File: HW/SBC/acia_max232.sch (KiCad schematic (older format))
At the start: 12 parts, among them J1 Serial Port, U4 MAX232, U5 6551

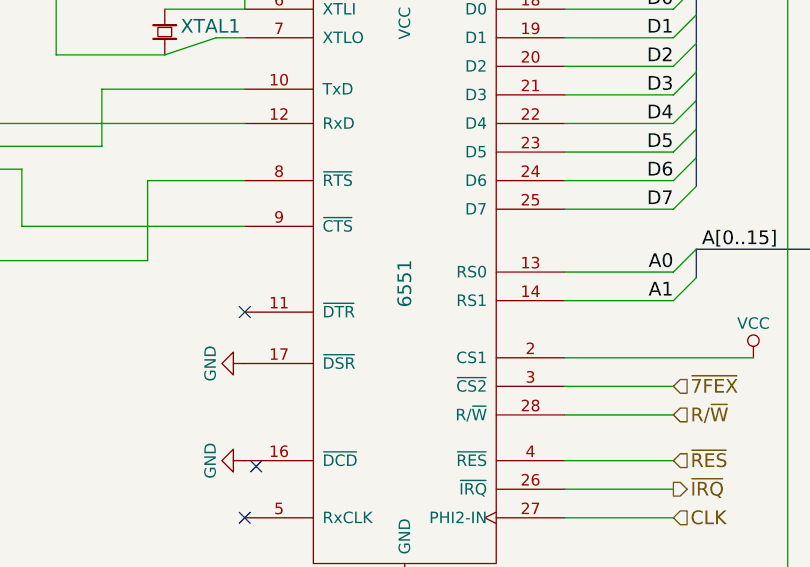
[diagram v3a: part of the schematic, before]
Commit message: Still no VCC net in PCBnew.
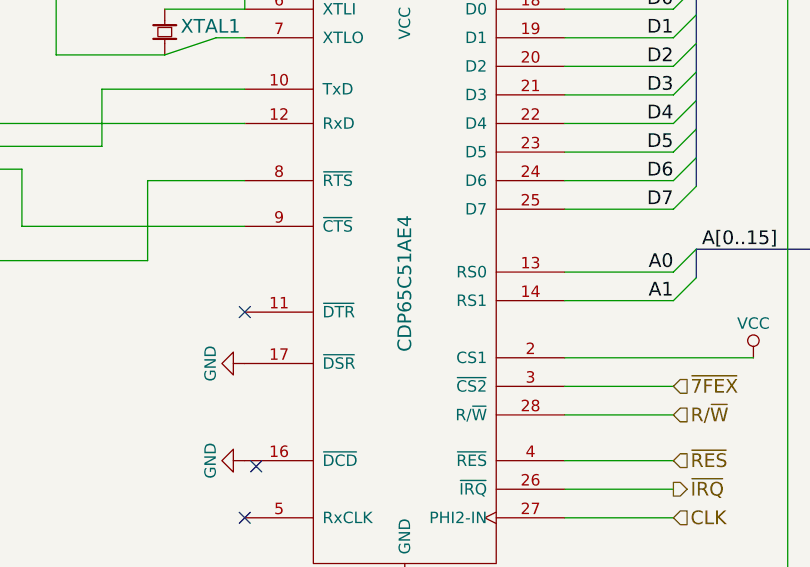
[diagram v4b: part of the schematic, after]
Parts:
- U4: footprint Housings_DIP:DIP-16_W7.62mm -> Housings_DIP:DIP-16_W7.62mm_Socket
- U5: value 6551 -> CDP65C51AE4; footprint Housings_DIP:DIP-28_W15.24mm -> Housings_DIP:DIP-28_W15.24mm_Socket
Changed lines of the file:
@@
 EESchema Schematic File Version 2
-LIBS:pluto-rescue
 LIBS:power
 LIBS:device
@@
 LIBS:pluto
 LIBS:pluto-cache
-LIBS:IDE_interface-cache
 EELAYER 25 0
 EELAYER END
@@
 P 7975 3150
 F 0 "U5" H 7750 4475 60  0000 C CNN
-F 1 "6551" V 7975 3150 60  0000 C CNN
-F 2 "Housings_DIP:DIP-28_W15.24mm" H 8025 2475 60  0001 C CNN
+F 1 "CDP65C51AE4" V 7975 3150 60  0000 C CNN
+F 2 "Housings_DIP:DIP-28_W15.24mm_Socket" H 8025 2475 60  0001 C CNN
 F 3 "" H 8025 2475 60  0001 C CNN
 	1    7975 3150
@@
 F 0 "U4" H 4950 2075 50  0000 R CNN
 F 1 "MAX232" H 4400 4200 50  0000 R CNN
-F 2 "Housings_DIP:DIP-16_W7.62mm" H 4550 2100 50  0001 L CNN
+F 2 "Housings_DIP:DIP-16_W7.62mm_Socket" H 4550 2100 50  0001 L CNN
 F 3 "" H 4500 3250 50  0001 C CNN
 	1    4500 3150

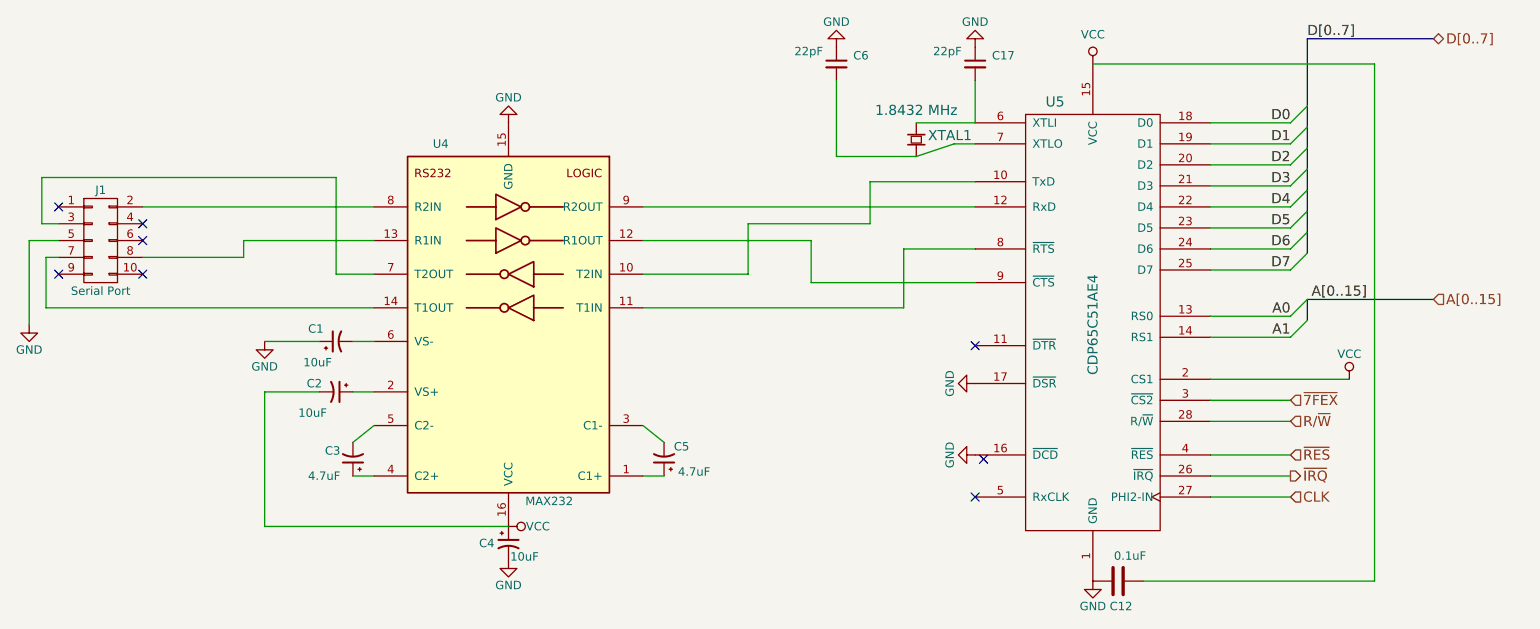
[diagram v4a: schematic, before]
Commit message: Schema is now Alpha.
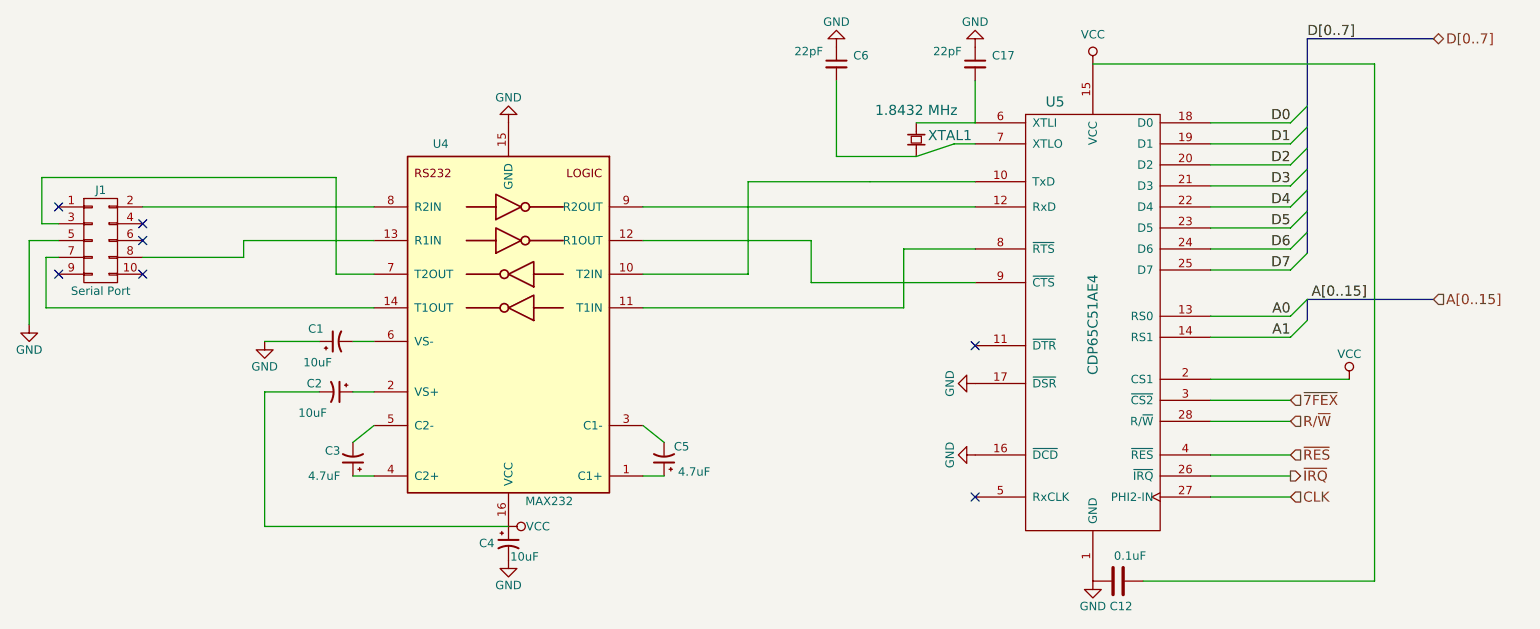
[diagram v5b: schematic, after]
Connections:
- no-connect marks 8 -> 7
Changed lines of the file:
@@
 $EndComp
 $Comp
-L VCC #PWR07
+L VCC #PWR18
 U 1 1 58D6F59A
 P 9500 3475
-F 0 "#PWR07" H 9500 3325 50  0001 C CNN
+F 0 "#PWR18" H 9500 3325 50  0001 C CNN
 F 1 "VCC" H 9500 3625 50  0000 C CNN
 F 2 "" H 9500 3475 50  0001 C CNN
@@
 $EndComp
 $Comp
-L GND #PWR08
+L GND #PWR12
 U 1 1 58D7044A
 P 6450 1500
-F 0 "#PWR08" H 6450 1250 50  0001 C CNN
+F 0 "#PWR12" H 6450 1250 50  0001 C CNN
 F 1 "GND" H 6450 1350 50  0000 C CNN
 F 2 "" H 6450 1500 50  0001 C CNN
@@
 $EndComp
 $Comp
-L GND #PWR09
+L GND #PWR8
 U 1 1 58D716F3
 P 3050 3250
-F 0 "#PWR09" H 3050 3000 50  0001 C CNN
+F 0 "#PWR8" H 3050 3000 50  0001 C CNN
 F 1 "GND" H 3050 3100 50  0000 C CNN
 F 2 "" H 3050 3250 50  0001 C CNN
@@
 $EndComp
 $Comp
-L GND #PWR010
+L GND #PWR7
 U 1 1 58D71F12
 P 1650 3150
-F 0 "#PWR010" H 1650 2900 50  0001 C CNN
+F 0 "#PWR7" H 1650 2900 50  0001 C CNN
 F 1 "GND" H 1650 3000 50  0000 C CNN
 F 2 "" H 1650 3150 50  0001 C CNN
@@
 $EndComp
 $Comp
-L GND #PWR011
+L GND #PWR11
 U 1 1 58D72DB3
 P 4500 4550
-F 0 "#PWR011" H 4500 4300 50  0001 C CNN
+F 0 "#PWR11" H 4500 4300 50  0001 C CNN
 F 1 "GND" H 4500 4400 50  0000 C CNN
 F 2 "" H 4500 4550 50  0001 C CNN
@@
 $EndComp
 $Comp
-L GND #PWR012
+L GND #PWR9
 U 1 1 58D73252
 P 4500 1950
-F 0 "#PWR012" H 4500 1700 50  0001 C CNN
+F 0 "#PWR9" H 4500 1700 50  0001 C CNN
 F 1 "GND" H 4500 1800 50  0000 C CNN
 F 2 "" H 4500 1950 50  0001 C CNN
@@
 NoConn ~ 1825 2450
 $Comp
-L GND #PWR013
+L GND #PWR15
 U 1 1 58D744C7
 P 7275 3925
-F 0 "#PWR013" H 7275 3675 50  0001 C CNN
+F 0 "#PWR15" H 7275 3675 50  0001 C CNN
 F 1 "GND" H 7275 3775 50  0000 C CNN
 F 2 "" H 7275 3925 50  0001 C CNN
@@
 $EndComp
 $Comp
-L GND #PWR014
+L GND #PWR14
 U 1 1 58D74507
 P 7275 3500
-F 0 "#PWR014" H 7275 3250 50  0001 C CNN
+F 0 "#PWR14" H 7275 3250 50  0001 C CNN
 F 1 "GND" H 7275 3350 50  0000 C CNN
 F 2 "" H 7275 3500 50  0001 C CNN
@@
 $EndComp
 $Comp
-L GND #PWR015
+L GND #PWR13
 U 1 1 59019537
 P 7275 1500
-F 0 "#PWR015" H 7275 1250 50  0001 C CNN
+F 0 "#PWR13" H 7275 1250 50  0001 C CNN
 F 1 "GND" H 7275 1350 50  0000 C CNN
 F 2 "" H 7275 1500 50  0001 C CNN
@@
 	0    1    1    0
 $EndComp
-NoConn ~ 7325 3950
 Wire Wire Line
 	8675 1950 9150 1950
@@
 	5300 2850 5925 2850
 Wire Wire Line
-	5925 2850 5925 2550
-Wire Wire Line
-	5925 2550 6650 2550
-Wire Wire Line
-	6650 2550 6650 2300
+	5925 2850 5925 2300
+Wire Wire Line
+	5925 2300 6650 2300
+Wire Wire Line
+	6650 2300 6650 2300
 Wire Wire Line
 	6925 2150 6450 2150
@@
 	3050 4350 4500 4350
 $Comp
-L GND #PWR016
+L GND #PWR17
 U 1 1 5924C9C7
 P 7975 4675
-F 0 "#PWR016" H 7975 4425 50  0001 C CNN
+F 0 "#PWR17" H 7975 4425 50  0001 C CNN
 F 1 "GND" H 7975 4525 50  0000 C CNN
 F 2 "" H 7975 4675 50  0001 C CNN
@@
 $EndComp
 $Comp
-L VCC #PWR017
+L VCC #PWR10
 U 1 1 5924CA70
 P 4500 4350
-F 0 "#PWR017" H 4500 4200 50  0001 C CNN
+F 0 "#PWR10" H 4500 4200 50  0001 C CNN
 F 1 "VCC" V 4500 4525 50  0000 C CNN
 F 2 "" H 4500 4350 50  0001 C CNN
@@
 $EndComp
 $Comp
-L VCC #PWR018
+L VCC #PWR16
 U 1 1 5924CC0E
 P 7975 1600
-F 0 "#PWR018" H 7975 1450 50  0001 C CNN
+F 0 "#PWR16" H 7975 1450 50  0001 C CNN
 F 1 "VCC" H 7975 1775 50  0000 C CNN
 F 2 "" H 7975 1600 50  0001 C CNN
@@
 CLK
 Wire Bus Line
-	9250 2725 9250 1450
+	9250 2725 9250 2600
+Wire Bus Line
+	9250 2600 9250 2475
+Wire Bus Line
+	9250 2475 9250 2350
+Wire Bus Line
+	9250 2350 9250 2225
+Wire Bus Line
+	9250 2225 9250 2100
+Wire Bus Line
+	9250 2100 9250 1975
+Wire Bus Line
+	9250 1975 9250 1850
+Wire Bus Line
+	9250 1850 9250 1450
 Wire Bus Line
 	9250 1450 10000 1450

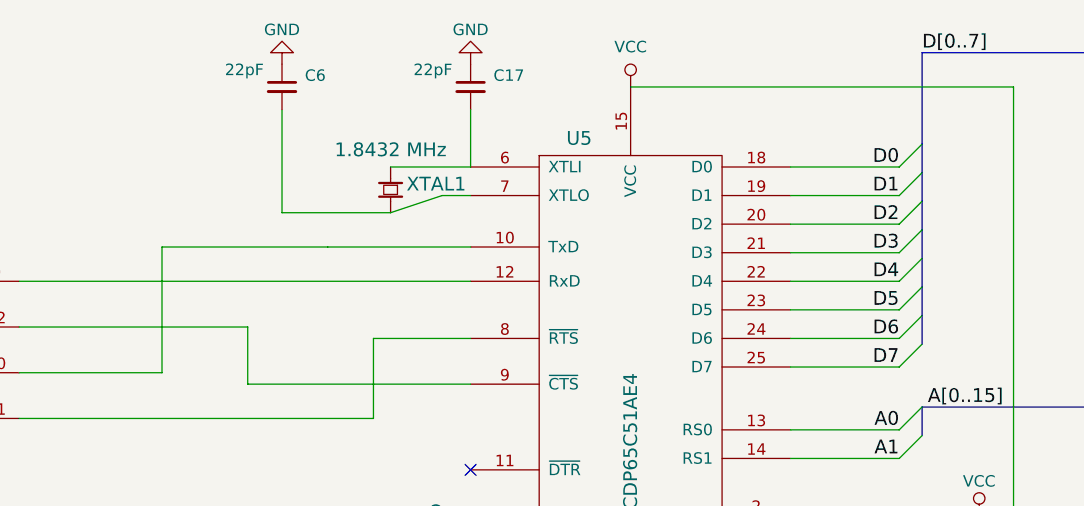
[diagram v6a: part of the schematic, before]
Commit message: Added ISR soft vector table initialisation.
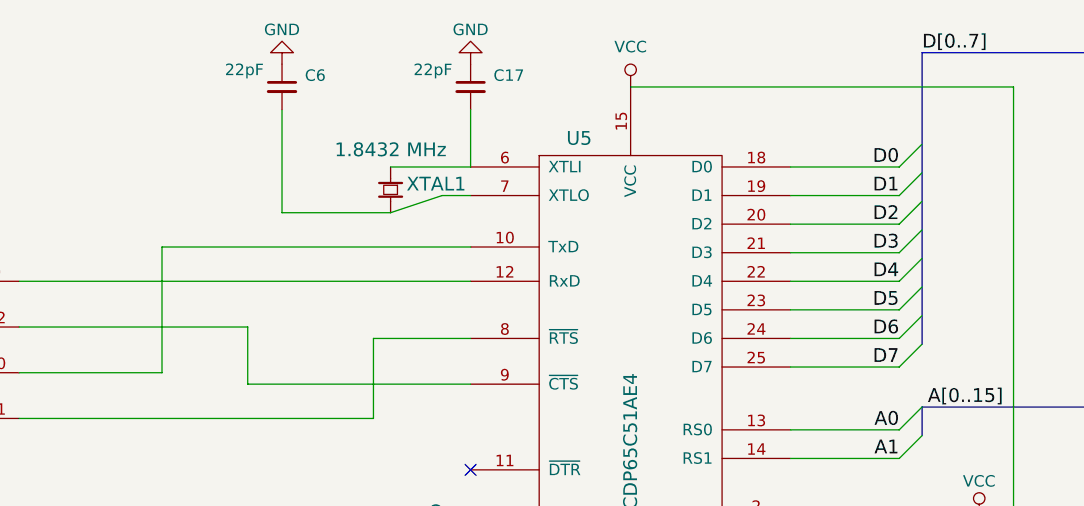
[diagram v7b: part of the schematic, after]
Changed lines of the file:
@@
 	5300 2450 7275 2450
 Wire Wire Line
-	6650 2300 7275 2300
+	5925 2300 7275 2300
 Wire Wire Line
 	5300 3050 6850 3050
@@
 Wire Wire Line
 	5925 2850 5925 2300
-Wire Wire Line
-	5925 2300 6650 2300
 Wire Wire Line
 	6650 2300 6650 2300
@@
 CLK
 Wire Bus Line
-	9250 2725 9250 2600
-Wire Bus Line
-	9250 2600 9250 2475
-Wire Bus Line
-	9250 2475 9250 2350
-Wire Bus Line
-	9250 2350 9250 2225
-Wire Bus Line
-	9250 2225 9250 2100
-Wire Bus Line
-	9250 2100 9250 1975
-Wire Bus Line
-	9250 1975 9250 1850
-Wire Bus Line
-	9250 1850 9250 1450
+	9250 1450 9250 2725
 Wire Bus Line
 	9250 1450 10000 1450
